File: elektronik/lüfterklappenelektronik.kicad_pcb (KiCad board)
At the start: 4 copper layers, 90 parts, among them J101 Conn_01x05_Male, J102 Ckmtw_2510S-2P, J103 Conn_LAN_ENC28J60, J104 USB_B_Micro, J106 WJ2EDGRC-5.08-2P, J107 WJ2EDGRC-5.08-2P, J108 WJ2EDGRC-5.08-2P, P101 PWR_BUS_CONN1, P103 PressureSensor3, P104 PressureSensor1, P105 PressureSensor2, P109 PWR_BUS_CONN2, Q101 IRLR8743TRPBF, Q102 IRLR8743TRPBF, Q103 IRLR8743TRPBF, Q104 Q_NPN_Darlington_BEC, Q105 Q_NPN_Darlington_BEC, SW101 SW_Push, SW102 SW_Push, U101 Gabellichtschranke, U102 Gabellichtschranke, U103 Gabellichtschranke, U105 ESP32-WROOM-32E, U106 AMS1117-3.3, U107 CP2102N-A01-GQFN28

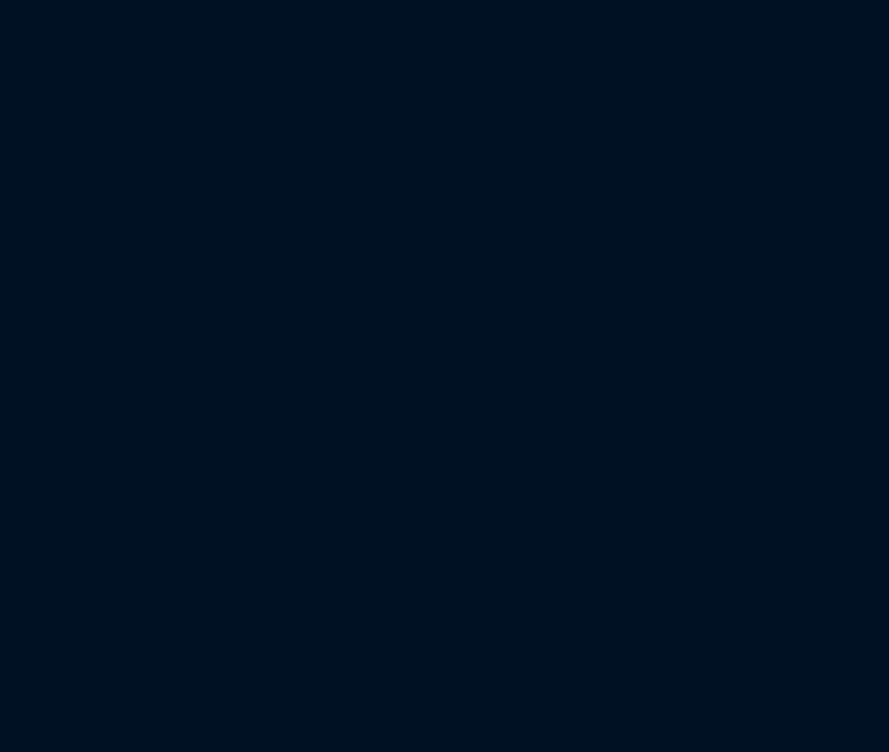
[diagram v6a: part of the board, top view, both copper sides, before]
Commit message: added more noise and transient protection
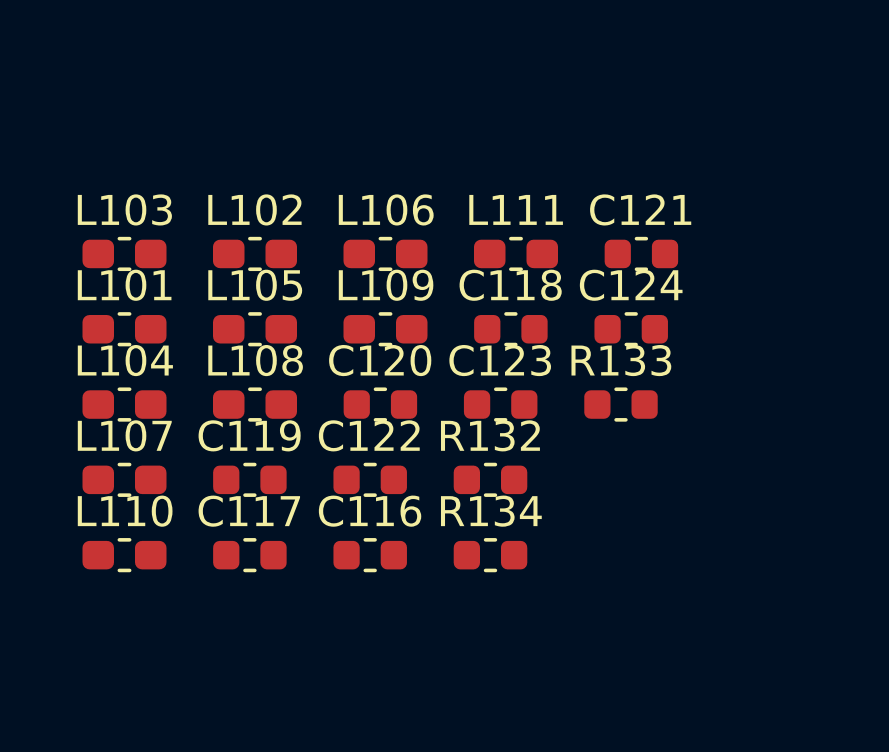
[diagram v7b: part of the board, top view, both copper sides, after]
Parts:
- added C116: 100P, Capacitor_SMD:C_0603_1608Metric, F.Cu at (36.5, 42.5)
- added C117: 100P, Capacitor_SMD:C_0603_1608Metric, F.Cu at (32.5, 42.5)
- added C118: 100P, Capacitor_SMD:C_0603_1608Metric, F.Cu at (41.2, 35.0)
- added C119: 100P, Capacitor_SMD:C_0603_1608Metric, F.Cu at (32.5, 40.0)
- added C120: 100P, Capacitor_SMD:C_0603_1608Metric, F.Cu at (36.9, 37.5)
- added C121: 100P, Capacitor_SMD:C_0603_1608Metric, F.Cu at (45.6, 32.5)
- added C122: 100P, Capacitor_SMD:C_0603_1608Metric, F.Cu at (36.5, 40.0)
- added C123: 100P, Capacitor_SMD:C_0603_1608Metric, F.Cu at (40.9, 37.5)
- added C124: 100P, Capacitor_SMD:C_0603_1608Metric, F.Cu at (45.2, 35.0)
- added L101: GZ1608D222TF, Inductor_SMD:L_0603_1608Metric_Pad1.05x0.95mm_HandSolder, F.Cu at (28.3, 35.0)
- added L102: GZ1608D222TF, Inductor_SMD:L_0603_1608Metric_Pad1.05x0.95mm_HandSolder, F.Cu at (32.7, 32.5)
- added L103: GZ1608D222TF, Inductor_SMD:L_0603_1608Metric_Pad1.05x0.95mm_HandSolder, F.Cu at (28.3, 32.5)
- added L104: GZ1608D222TF, Inductor_SMD:L_0603_1608Metric_Pad1.05x0.95mm_HandSolder, F.Cu at (28.3, 37.5)
- added L105: GZ1608D222TF, Inductor_SMD:L_0603_1608Metric_Pad1.05x0.95mm_HandSolder, F.Cu at (32.7, 35.0)
- added L106: GZ1608D222TF, Inductor_SMD:L_0603_1608Metric_Pad1.05x0.95mm_HandSolder, F.Cu at (37.0, 32.5)
- added L107: GZ1608D222TF, Inductor_SMD:L_0603_1608Metric_Pad1.05x0.95mm_HandSolder, F.Cu at (28.3, 40.0)
- added L108: GZ1608D222TF, Inductor_SMD:L_0603_1608Metric_Pad1.05x0.95mm_HandSolder, F.Cu at (32.7, 37.5)
- added L109: GZ1608D222TF, Inductor_SMD:L_0603_1608Metric_Pad1.05x0.95mm_HandSolder, F.Cu at (37.0, 35.0)
- added L110: GZ1608D222TF, Inductor_SMD:L_0603_1608Metric_Pad1.05x0.95mm_HandSolder, F.Cu at (28.3, 42.5)
- added L111: GZ1608D222TF, Inductor_SMD:L_0603_1608Metric_Pad1.05x0.95mm_HandSolder, F.Cu at (41.4, 32.5)
- added R132: 5K6(1%), Resistor_SMD:R_0603_1608Metric, F.Cu at (40.5, 40.0)
- added R133: 5K6(1%), Resistor_SMD:R_0603_1608Metric, F.Cu at (44.9, 37.5)
- added R134: 10K(5%), Resistor_SMD:R_0603_1608Metric, F.Cu at (40.5, 42.5)
- R101, R102, R103: value 43(1%) -> 91(1%)
- R104, R105, R106: value 2K2 -> 5K6(1%)
- R109, R110, R111: value 100(1%) -> 91(1%)
- R118, R119, R120, R121: value 22(1%) -> 220(1%)
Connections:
- D106 pad 1: Net-(D106-Pad1) -> Net-(C121-Pad1)
- D106 pad 2: /EndstopDamper1 -> Net-(D106-Pad2)
- D107 pad 1: Net-(D107-Pad1) -> Net-(C119-Pad1)
- D107 pad 2: /EndstopDamper2 -> Net-(D107-Pad2)
- D108 pad 1: Net-(D108-Pad1) -> Net-(C120-Pad1)
- D108 pad 2: /EndstopDamper3 -> Net-(D108-Pad2)
- J102 pad 2: Net-(D104-Pad1) -> Net-(J102-Pad2)
- P103 pad 1: +3V3 -> Net-(L109-Pad1)
- P104 pad 1: +3V3 -> Net-(L107-Pad1)
- P105 pad 1: +3V3 -> Net-(L108-Pad1)
- R101 pad 2: Net-(R101-Pad2) -> Net-(C116-Pad1)
- R102 pad 2: Net-(R102-Pad2) -> Net-(C117-Pad1)
- R103 pad 2: Net-(R103-Pad2) -> Net-(C118-Pad1)
- R104 pad 1: Net-(R104-Pad1) -> /EndstopDamper1
- R104 pad 2: GND -> Net-(D106-Pad2)
- R105 pad 1: Net-(R105-Pad1) -> /EndstopDamper2
- R105 pad 2: GND -> Net-(D107-Pad2)
- R106 pad 1: Net-(R106-Pad1) -> /EndstopDamper3
- R106 pad 2: GND -> Net-(D108-Pad2)
- R118 pad 2: /PJON -> Net-(L111-Pad2)
- U101 pad 1: Net-(R101-Pad2) -> Net-(L101-Pad1)
- U101 pad 3: Net-(D106-Pad1) -> Net-(L104-Pad2)
- U101 pad 4: Net-(R104-Pad1) -> GND
- U102 pad 1: Net-(R102-Pad2) -> Net-(L102-Pad1)
- U102 pad 3: Net-(D107-Pad1) -> Net-(L105-Pad2)
- U102 pad 4: Net-(R105-Pad1) -> GND
- U103 pad 1: Net-(R103-Pad2) -> Net-(L103-Pad1)
- U103 pad 3: Net-(D108-Pad1) -> Net-(L106-Pad2)
- U103 pad 4: Net-(R106-Pad1) -> GND
- U105 pad 10: /FAN -> Net-(R118-Pad1)
- U105 pad 9: Net-(R118-Pad1) -> /FAN

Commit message: placing mostly done
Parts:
- removed C123, C124: 100P, Capacitor_SMD:C_0603_1608Metric
- removed L108, L109: GZ1608D222TF, Inductor_SMD:L_0603_1608Metric_Pad1.05x0.95mm_HandSolder
- added C125: 100P, Capacitor_SMD:C_0603_1608Metric, F.Cu at (100.3, 123.2)
- added C126: 100P, Capacitor_SMD:C_0603_1608Metric, F.Cu at (86.4, 87.6)
- added C127: 100P, Capacitor_SMD:C_0603_1608Metric, F.Cu at (119.4, 133.3)
- added C128: 100P, Capacitor_SMD:C_0603_1608Metric, F.Cu at (119.4, 105.4)
- added C129: 100P, Capacitor_SMD:C_0603_1608Metric, F.Cu at (109.2, 105.4)
- added R135: 5K6(1%), Resistor_SMD:R_0603_1608Metric, F.Cu at (99.1, 115.6)
- moved R112 163.6 mm to (119.4, 74.9), turned to 270 degrees
- moved D105 159.5 mm to (118.1, 71.1)
- moved L107 131.8 mm to (139.7, 110.5), turned to 270 degrees
- moved D114 129.7 mm to (135.9, 69.8)
- moved L103 125.8 mm to (115.6, 123.2), turned to 90 degrees
- moved L106 123.3 mm to (120.7, 123.2), turned to 270 degrees
- moved C120 122.5 mm to (124.5, 123.2), turned to 270 degrees
- moved Q105 122.3 mm to (68.6, 80.0), turned to 90 degrees
- moved D117 121.7 mm to (123.2, 64.8), turned to 180 degrees
- moved R118 120.2 mm to (90.2, 72.4), turned to 270 degrees
- moved C118 117.0 mm to (118.1, 123.2), turned to 270 degrees
- moved C121 112.4 mm to (95.2, 133.3), turned to 180 degrees
- moved R133 110.5 mm to (123.2, 115.6)
- moved R116 110.5 mm to (68.6, 74.9)
- moved C122 110.3 mm to (124.5, 106.7), turned to 90 degrees
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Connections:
- D104 pad 1: Net-(D104-Pad1) -> GND
- D104 pad 2: GND -> Net-(C129-Pad1)
- J102 pad 2: Net-(J102-Pad2) -> Net-(C129-Pad1)
- L110 pad 1: Net-(J102-Pad2) -> Net-(C129-Pad1)
- L110 pad 2: Net-(D104-Pad1) -> Net-(C128-Pad1)
- P103 pad 1: Net-(L109-Pad1) -> Net-(L107-Pad1)
- P105 pad 1: Net-(L108-Pad1) -> Net-(L107-Pad1)
- R107 pad 1: Net-(D104-Pad1) -> Net-(C128-Pad1)
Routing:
- net /UCD-: track 10.7 -> 2.58 mm
- net /UCD+: track 9.87 -> 2.58 mm
- added copper zone on In2.Cu, net +3V3
- added copper zone on B.Cu, net GND
- added copper zone on In1.Cu, net GND
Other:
- board outline added: 80 x 87.6 mm
- board text added: "5V | 12V"
- board text added: "BMP1"
- board text added: "BMP2"
- board text added: "BMP3"
- board text added: "D1 Endstop"
- board text added: "D2 Endstop"
- board text added: "D3 Endstop"
- board text removed: "12V | 5V"
- board text removed: "Damper1 Endstop"
- board text removed: "Damper3ES"
- board text removed: "Endstop Damper2"
- board text removed: "Pressure1"
- board text removed: "Pressure2"
- board text removed: "Pressure3"
